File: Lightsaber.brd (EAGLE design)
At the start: 210 x 10 mm, 25 parts

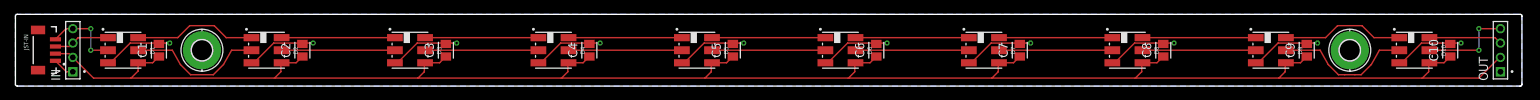
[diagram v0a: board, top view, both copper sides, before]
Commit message: fixed silkscreen for names/values
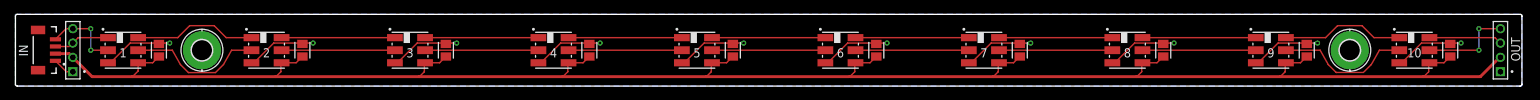
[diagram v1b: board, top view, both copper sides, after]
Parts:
- renumbered D1 to 1, D10 to 10, D2 to 2, D3 to 3, D4 to 4, D5 to 5, D6 to 6, D7 to 7, D8 to 8, D9 to 9
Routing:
- net VCC: track 262.1 -> 259.0 mm
